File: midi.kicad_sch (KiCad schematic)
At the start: 15 parts, among them J501 Conn_01x06

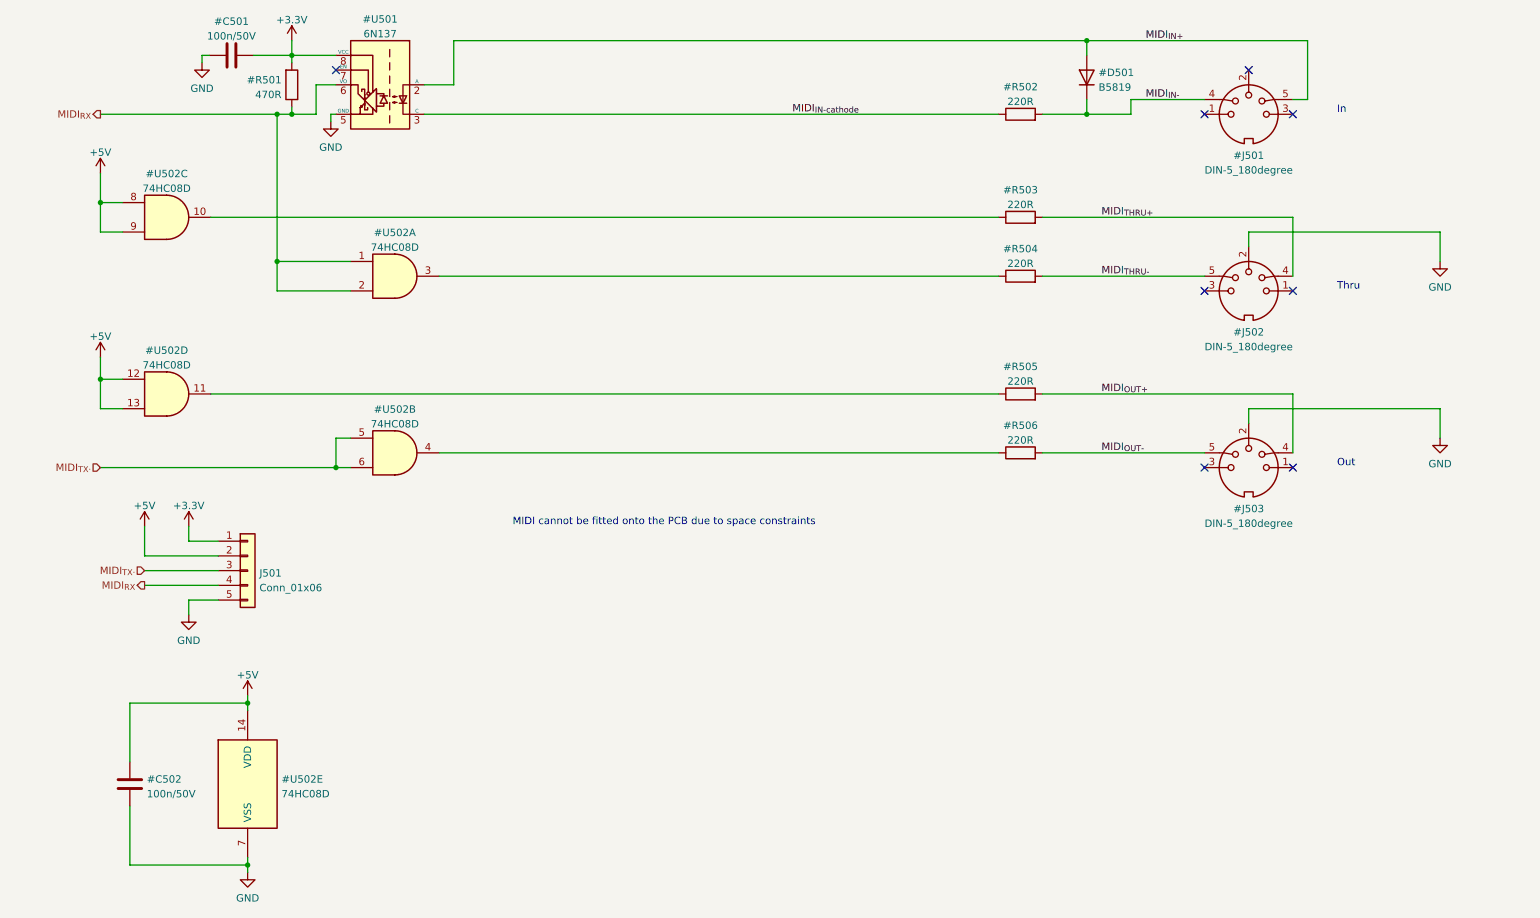
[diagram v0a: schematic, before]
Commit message: Added Testpoints
Schematic and PCB updated
Also probably some other smaller changes that I forgot about
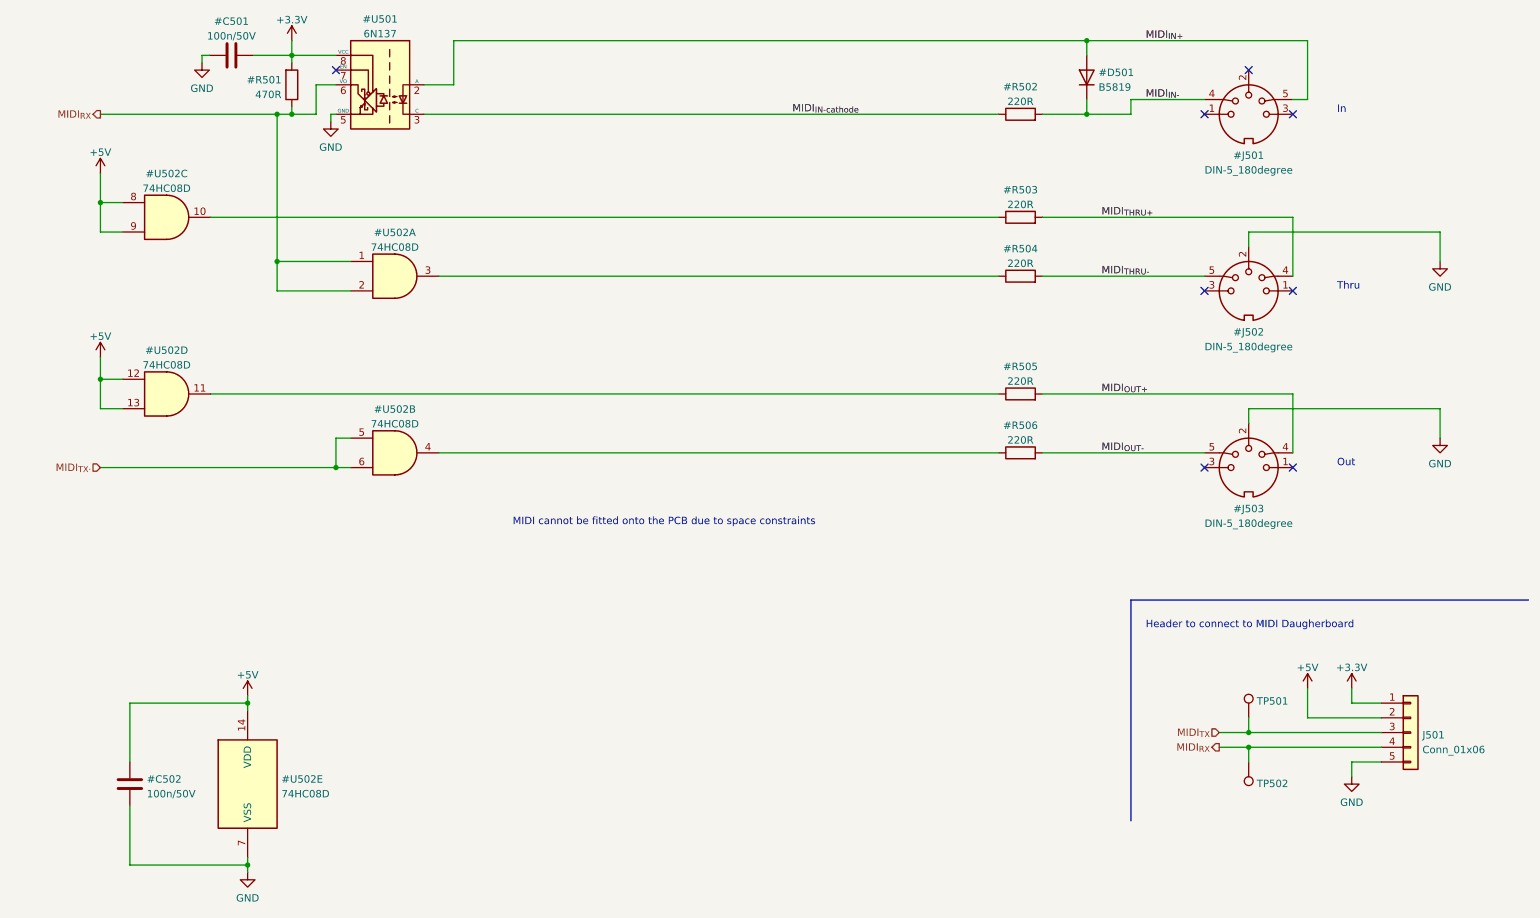
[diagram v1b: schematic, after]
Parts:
- added TP501, TP502: TestPoint, TestPoint:TestPoint_Loop_D1.80mm_Drill1.0mm_Beaded, symbol Connector:TestPoint
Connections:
- net MIDI_{RX}: now also TP502.1
- net MIDI_{TX·}: no longer J501.3 (Pin_3)
- new net MIDI_{TX}: J501.3 (Pin_3), TP501.1
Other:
- note added: "Header to connect to MIDI Daugherboard"
- moved on the sheet: J501

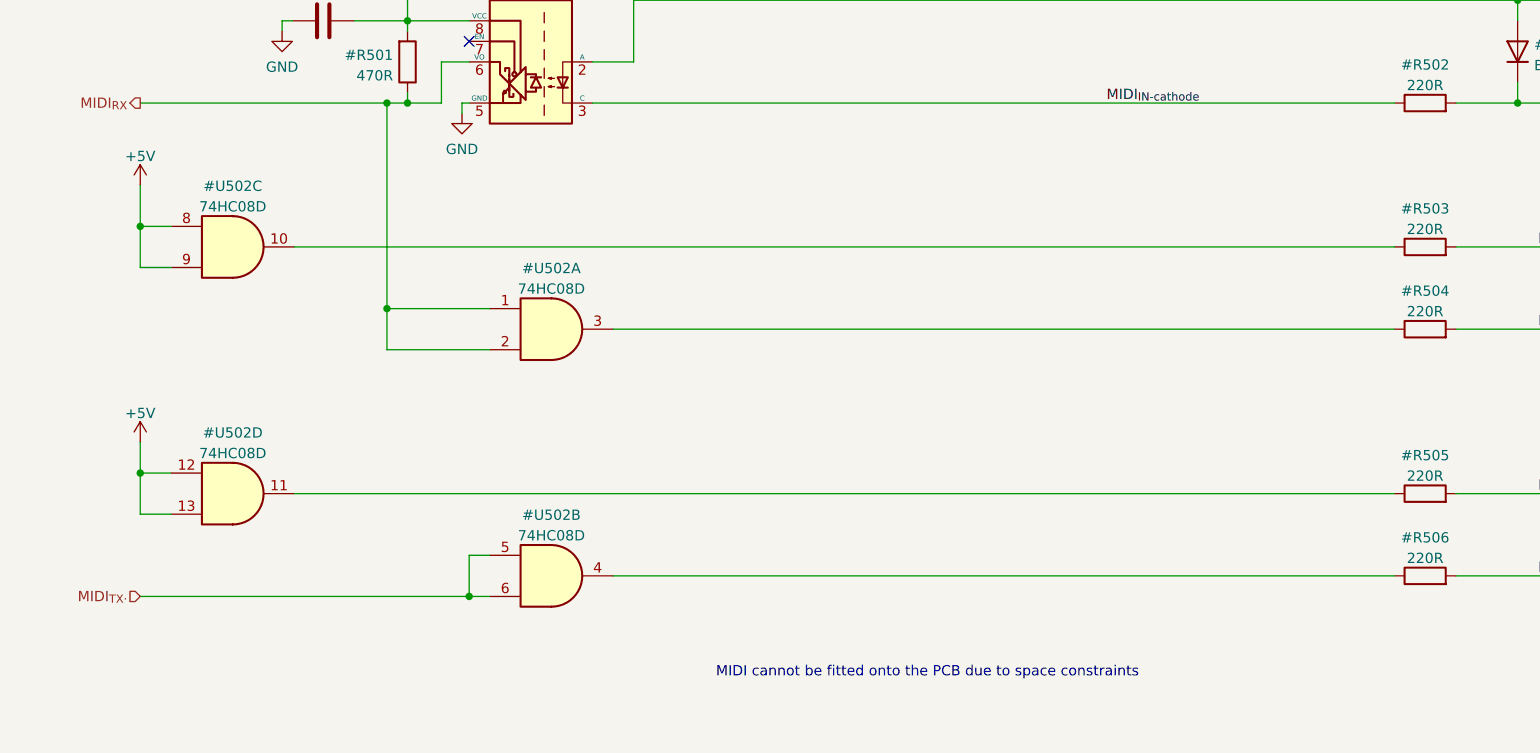
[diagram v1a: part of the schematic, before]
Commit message: Fix DRCs and BOM errors
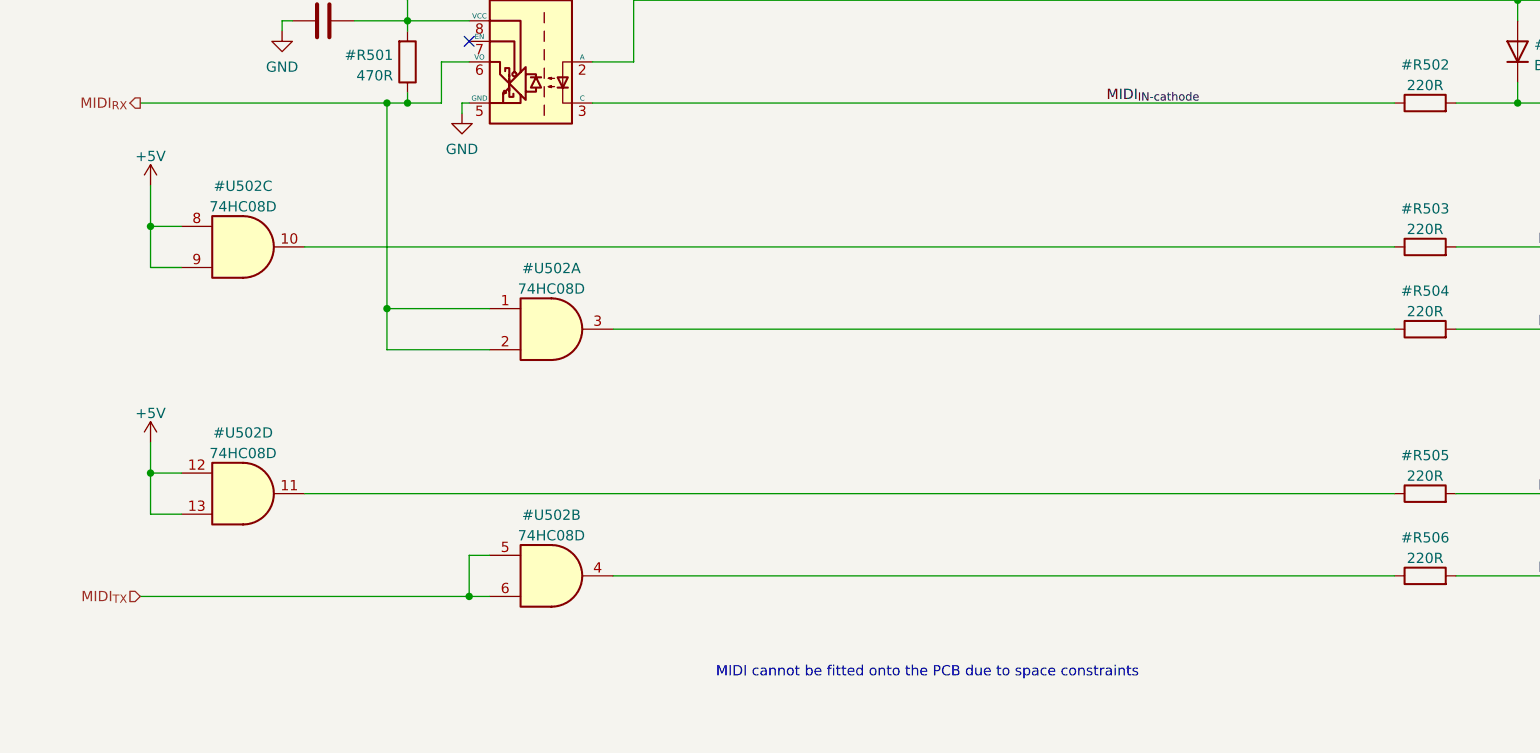
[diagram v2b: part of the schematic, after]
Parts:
- J501: LCSC (none) -> C37208
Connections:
- net MIDI_{TX·} is gone; now on net MIDI_{TX}: #U502.5, #U502.6
